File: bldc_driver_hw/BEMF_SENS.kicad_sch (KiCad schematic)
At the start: 4 parts, among them U12 LM397

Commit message: wip
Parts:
- removed R51, R52, R53: R_Small, symbol Device:R_Small
- added C41, C80, C82: 10uF, Capacitor_SMD:C_0805_2012Metric_Pad1.18x1.45mm_HandSolder, symbol Device:C_Small
- added C42, C81, C83: 100nF, Capacitor_SMD:C_0603_1608Metric_Pad1.08x0.95mm_HandSolder, symbol Device:C_Small
- added R78, R79, R80, R81, R82, R83, R84, R85, R86: R_Small, symbol Device:R_Small
- added U13, U14: LM397, Package_TO_SOT_SMD:SOT-23-5, symbol Comparator:LM397
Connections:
- net BEMF_U: now also U12.4
- net BEMF_V: now also U14.4
- net BEMF_W: now also U13.4
- net GND: now also C41.2, C42.2, C80.2, C81.2, C82.2, C83.2, R79.2, R81.2, R85.2, U13.2 (V-), U14.2 (V-)
- net PHASE_U: now also R78.1
- net PHASE_V: now also R84.1
- net PHASE_W: now also R80.1
- net V_BEMF: now also R82.2, R83.2, R86.2, U13.1 (-), U14.1 (-)
- net at U12.3 (+): now also R78.2, R79.1, R82.1
- net +3.3V: now reaches U12.5 (V+)
- net +3.3V: now also C41.1, C42.1, C80.1, C81.1, C82.1, C83.1, U13.5 (V+), U14.5 (V+)
- new net: R80.2, R81.1, R83.1, U13.3 (+)
- new net: R84.2, R85.1, R86.1, U14.3 (+)
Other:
- moved on the sheet: U12

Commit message: schematic finished pcb in progress
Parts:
- removed C81, C83: 100nF, Capacitor_SMD:C_0603_1608Metric_Pad1.08x0.95mm_HandSolder, symbol Device:C_Small
- removed C82: 10uF, Capacitor_SMD:C_0805_2012Metric_Pad1.18x1.45mm_HandSolder, symbol Device:C_Small
- removed R80, R81: R_Small, symbol Device:R_Small
- removed U12, U13, U14: LM397, Package_TO_SOT_SMD:SOT-23-5, symbol Comparator:LM397
- added C78, C79: 27nF, Capacitor_SMD:C_0603_1608Metric, symbol Device:C_Small
- added R100, R98, R99: 10k, Resistor_SMD:R_0603_1608Metric, symbol Device:R_Small
- added R86: 47k, Resistor_SMD:R_0603_1608Metric, symbol Device:R_Small
- added R87: 3k, Resistor_SMD:R_0603_1608Metric, symbol Device:R_Small
- added R89: 100k, Resistor_SMD:R_0603_1608Metric, symbol Device:R
- added R92, R93, R94, R95, R96, R97: R_Small, Resistor_SMD:R_0603_1608Metric, symbol Device:R_Small
- added U13: MCP6569, Package_SO:SOIC-14_3.9x8.7mm_P1.27mm, symbol Comparator:MCP6569
- C80: value 10uF -> 27nF; footprint Capacitor_SMD:C_0805_2012Metric_Pad1.18x1.45mm_HandSolder -> Capacitor_SMD:C_0603_1608Metric; now not fitted
- R82: renamed from R78; value R_Small -> 47k; footprint (none) -> Resistor_SMD:R_0603_1608Metric
- R83: renamed from R79; value R_Small -> 3k; footprint (none) -> Resistor_SMD:R_0603_1608Metric
- R84: value R_Small -> 47k; footprint (none) -> Resistor_SMD:R_0603_1608Metric
- R85: value R_Small -> 3k; footprint (none) -> Resistor_SMD:R_0603_1608Metric
- R88: renamed from R82; value R_Small -> 100k; footprint (none) -> Resistor_SMD:R_0603_1608Metric
- R90: renamed from R83; value R_Small -> 100k; footprint (none) -> Resistor_SMD:R_0603_1608Metric
- R91: renamed from R86; value R_Small -> 100k; footprint (none) -> Resistor_SMD:R_0603_1608Metric
- renumbered C41 to C81, C42 to C82
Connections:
- net +3.3V: now also R100.1, R98.1, R99.1, U13.4 (V+); no longer C80.1
- net BEMF_U: now also R100.2, R96.1, U13.1
- net BEMF_V: now also R95.1, R99.2, U13.8
- net BEMF_W: now also R97.1, R98.2, U13.7
- net GND: now also C78.2, C79.2, R87.2, U13.11 (V-)
- net PHASE_W: now also R86.1
- net V_BEMF: now also U13.2 (-), U13.6 (-), U13.9 (-)
- net at R82.2, R83.1, R88.1: now also C78.1, R93.2
- net at R90.1: now also C80.1, R86.2, R87.1, R94.2
- net at R84.2, R85.1, R91.1: now also C79.1, R92.2
- new net: R92.1, R95.2, U13.10 (+)
- new net: R94.1, R97.2, U13.5 (+)
- new net: R93.1, R96.2, U13.3 (+)
- no-connect marks 0 -> 3
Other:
- moved on the sheet: C81, C82, R90, R91

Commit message: Board finished to review
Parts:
- removed R89: 100k, Resistor_SMD:R_0603_1608Metric, symbol Device:R
- C81: footprint Capacitor_SMD:C_0805_2012Metric_Pad1.18x1.45mm_HandSolder -> Capacitor_SMD:C_0603_1608Metric
- C82: footprint Capacitor_SMD:C_0603_1608Metric_Pad1.08x0.95mm_HandSolder -> Capacitor_SMD:C_0603_1608Metric
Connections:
- net BEMF_V: now also R97.1, R98.2; no longer R95.1, R99.2
- net BEMF_W: now also R95.1, R99.2, U13.14; no longer R97.1, R98.2, U13.7
- net PHASE_V: now also R86.1; no longer R84.1
- net PHASE_W: now also R84.1; no longer R86.1
- net V_BEMF: now also U13.13 (-); no longer U13.6 (-)
- net at R92.1, R95.2: now also U13.12 (+); no longer U13.10 (+)
- net at R94.1, R97.2: now also U13.10 (+); no longer U13.5 (+)
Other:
- moved on the sheet: U13B, U13C, U13D

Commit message: wip
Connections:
- net BEMF_U: now also U13.7; no longer U13.1
- net BEMF_V: now also R95.1, R99.2, U13.14; no longer R97.1, R98.2, U13.8
- net BEMF_W: now also R97.1, R98.2, U13.8; no longer R95.1, R99.2, U13.14
- net PHASE_V: now also R84.1; no longer R86.1
- net PHASE_W: now also R86.1; no longer R84.1
- net V_BEMF: now also U13.6 (-); no longer U13.2 (-)
- net at U13.5 (+): now also R93.1, R96.2
- now unconnected: U13.3 (+)
- no-connect marks 3 -> 0
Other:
- moved on the sheet: U13A, U13B
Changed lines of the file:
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@@
 	)
 	(junction
-		(at 148.59 52.07)
+		(at 182.88 24.13)
 		(diameter 0)
 		(color 0 0 0 0)
 	)
 	(junction
-		(at 182.88 24.13)
+		(at 127 49.53)
 		(diameter 0)
 		(color 0 0 0 0)
@@
 	)
 	(junction
-		(at 127 49.53)
+		(at 109.22 114.3)
 		(diameter 0)
 		(color 0 0 0 0)
 	)
 	(junction
-		(at 109.22 114.3)
+		(at 148.59 52.07)
 		(diameter 0)
 		(color 0 0 0 0)
 	)
-	(no_connect
-		(at 154.94 139.7)
-	)
-	(no_connect
-		(at 139.7 142.24)
-	)
-	(no_connect
-		(at 139.7 137.16)
-	)
 	(wire
 		(pts
@@
 	(wire
 		(pts
-			(xy 114.3 54.61) (xy 133.35 54.61)
-		)
-		(stroke
-			(width 0)
-			(type default)
-		)
-	)
-	(wire
-		(pts
 			(xy 96.52 107.95) (xy 83.82 107.95)
 		)
@@
 	(wire
 		(pts
-			(xy 125.73 49.53) (xy 127 49.53)
-		)
-		(stroke
-			(width 0)
-			(type default)
-		)
-	)
-	(wire
-		(pts
 			(xy 127 106.68) (xy 127 114.3)
 		)
@@
 	(wire
 		(pts
+			(xy 114.3 54.61) (xy 132.08 54.61)
+		)
+		(stroke
+			(width 0)
+			(type default)
+		)
+	)
+	(wire
+		(pts
 			(xy 154.94 109.22) (xy 154.94 116.84)
 		)
@@
 	(wire
 		(pts
-			(xy 97.79 78.74) (xy 97.79 81.28)
+			(xy 127 49.53) (xy 132.08 49.53)
 		)
 		(stroke
@@
 	(wire
 		(pts
-			(xy 162.56 52.07) (xy 156.21 52.07)
+			(xy 97.79 78.74) (xy 97.79 81.28)
 		)
 		(stroke
@@
 	(wire
 		(pts
-			(xy 96.52 107.95) (xy 96.52 110.49)
+			(xy 162.56 52.07) (xy 156.21 52.07)
 		)
 		(stroke
@@
 	(wire
 		(pts
-			(xy 142.24 41.91) (xy 148.59 41.91)
+			(xy 96.52 107.95) (xy 96.52 110.49)
 		)
 		(stroke
@@
 	(wire
 		(pts
-			(xy 127 49.53) (xy 133.35 49.53)
+			(xy 142.24 41.91) (xy 148.59 41.91)
 		)
 		(stroke
@@
 	(wire
 		(pts
+			(xy 125.73 49.53) (xy 127 49.53)
+		)
+		(stroke
+			(width 0)
+			(type default)
+		)
+	)
+	(wire
+		(pts
 			(xy 156.21 52.07) (xy 148.59 52.07)
 		)
@@
 	(wire
 		(pts
+			(xy 147.32 52.07) (xy 148.59 52.07)
+		)
+		(stroke
+			(width 0)
+			(type default)
+		)
+	)
+	(wire
+		(pts
 			(xy 82.55 83.82) (xy 82.55 81.28)
 		)
@@
 			"AAAAAAAJAAAANwADAAgAAAAKAAAA+AACAAwAAAA9AAQABwAAACYAAAAKAAAAPQAEAAcAAAAnAAAA"
 			"CgAAAJQABQAGAAAAKAAAACYAAAAnAAAAuAAFACoAAAArAAAAKAAAACkAAAD3AAMALQAAAAAAAAD6"
-			"AAQAKwAAACwAAAA0AAAA+AACACwAAAA9AAQALg=="
+			"AAQAKwAAACwAAAA0AAAA+AACACwAAAA9AAQALgAAAAAAAAAAAAAAAAAAAAAAAAAAAAAAAAAAAAAA"
+			"AAAAAAAAAAAAAAAAAAAAAAAAAAAAAAAAAAAAAAAAAAAAAAAAAAAAAAAAAAAAAAAAAAAAAAAAAAAA"
+			"AAAAAAAAAAAAAAAAAAAAAAAAAAAAAAAAAAAAAAAAAAAAAAAAAAAAAAAAAAAAAAAAAAAAAAAAAAAA"
+			"AAAAAAAAAAAAAAAAAAAAAAAAAAAAAAAAAAAAAAAAAAAAAAAAAAAAAAAAAAAAAAAAAAAAAAAAAAAA"
+			"AAAAAAAAAAAAAAAAAAAAAAAAAAAAAAAAAAAAAAAAAAAAAAAAAAAAAAAAAAAAAAAAAAAAAAAAAAAA"
+			"AAAAAAAAAAAAAAAAAAAAAAAAAAAAAAAAAAAAAAAAAAAAAAAAAAAAAAAAAAAAAAAAAAAAAAAAAAAA"
+			"AAAAAAAAAAAAAAAAAAAAAAAAAAAAAAAAAAAAAAAAAAAAAAAAAAAAAAAAAAAAAAAAAAAAAAAAAAAA"
+			"AAAAAAAAAAAAAAAAAAAAAAAAAAAAAAAAAAAAAAAAAAAAAAAAAAAAAAAAAAAAAAAAAAAAAAAAAAAA"
+			"AAAAAAAAAAAAAAAAAAAAAAAAAAAAAAAAAAAAAAAAAAAAAAAAAAAAAAAAAAAAAAAAAAAAAAAAAAAA"
+			"AAAAAAAAAAAAAAAAAAAAAAAAAAAAAAAAAAAAAAAAAAAAAAAAAAAAAAAAAAAAAAAAAAAAAAAAAAAA"
+			"AAAAAAAAAAAAAAAAAAAAAAAAAAAAAAAAAAAAAAAAAAAAAAAAAAAAAAAAAAAAAAAAAAAAAAAAAAAA"
+			"AAAAAAAAAAAAAAAAAAAAAAAAAAAAAAAAAAAAAAAAAAAAAAAAAAAAAAAAAAAAAAAAAAAAAAAAAAAA"
+			"AAAAAAAAAAAAAAAAAAAAAAAAAAAAAAAAAAAAAAAAAAAAAAAAAAAAAAAAAAAAAAAAAAAAAAAAAAAA"
+			"AAAAAAAAAAAAAAAAAAAAAAAAAAAAAAAAAAAAAAAAAAAAAAAAAAAAAAAAAAAAAAAAAAAAAAAAAAAA"
+			"AAAAAAAAAAAAAAAAAAAAAAAAAAAAAAAAAAAAAAAAAAAAAAAAAAAAAAAAAAAAAAAAAAAAAAAAAAAA"
+			"AAAAAAAAAAAAAAAAAAAAAAAAAAAAAAAAAAAAAAAAAAAAAAAAAAAAAAAAAAAAAAAAAAAAAAAAAAAA"
+			"AAAAAAAAAAAAAAAAAAAAAAAAAAAAAAAAAAAAAAAAAAAAAAAAAAAAAAAAAAAAAAAAAAAAAAAAAAAA"
+			"AAAAAAAAAAAAAAAAAAAAAAAAAAAAAAAAAAAAAAAAAAAAAAAAAAAAAAAAAAAAAAAAAAAAAAAAAAAA"
+			"AAAAAAAAAAAAAAAAAAAAAAAAAAAAAAAAAAAAACoqACoqKgAqKioAKioqACoqKgCCfoLEgn6C0oN9"
+			"gzgqKioAKioqACoqKgAqKioAKioqACoqKgAqKioAKioqACoqKgAqKioAKioqACoqKgAqKioAKioq"
+			"ACoqKgAqKioAKioqACoqKgBwcQAAAAAAAFAAAAAAAAAAawotzR5cAAAAAAAAXH4AAMC6nQwbXAAA"
+			"AAAAAAAAAAAAAAAAAADwPwAAAAAAAAAAAAAAAAAAAAAQAAAAEAAAACAAAAAAAAAAEQQAAAAAAACg"
+			"p5wMG1wAAEArCA4bXAAAAAAAAAAAAAAAAAAAAAAAAIlTXSAqKioAKioqACoqKgAqKioAKioqACoq"
+			"KgAqKioAKioqAJCQkAGCfoL/gn6C/YJ+gt6Cf4JCKioqAIpRXKeKUVynKioqACoqKgAqKioAKioq"
+			"ACoqKgAqKioAKioqACoqKgCQkJABgn6C/4J+gmuCfoKrgn6C/oJ+gpmJVV+vilJcqioqKgAqKioA"
+			"KioqACoqKgAqKioAKioqACoqKgCDfoKOgn6CqoJ+gv+DfoNmKioqAIJ+glWCfoLqg3t/9odja8Iq"
+			"KioAKioqACoqKgAqKioAKioqACoqKgAqKioAg36CjoJ+gqqCfoL/g36DZioqKgAqKioAhH6EEYN7"
+			"f6aCfoL/gn6CqoR/hBIqKioAKioqACoqKgAqKioAKioqACoqKgCQkJABgn6C/4J+glWCfoKrg36C"
+			"zIN+gsyDfYMhgn6CTIJ+guSCfoLmg36BTyoqKgAqKioAKioqACoqKgAqKioAkJCQAYJ+gv+CfoJV"
+			"gX+BK4J+gjOCfoIzg4ODCCoqKgCDfIMQgn6CmYJ+gv+CfoKqhYCAEyoqKgAqKioAKioqAJCQkAGC"
+			"foL/gn6CVSoqKgAqKioAKioqACoqKgAqKioAKioqACoqKgCCf4JOgn6C5oJ+gvKCfoK5g36Cjioq"
+			"KgCQkJABgn6C/4J+glUqKioAgn6C14N+gykqKioAKioqACoqKgAqKioAgn+CToJ+guaCfoLygn6C"
+			"uYN+go4qKioAkJCQAYJ+gv+CfoJWgn6C3YJ+gvqCfoLign6CRSoqKgCDfIMQgn6CmYJ+gv+CfoKq"
+			"hYCAEyoqKgAqKioAKioqAJCQkAGCfoL/gn6CVYR+gSKDfoLcgn2BRoGBgQ6CfoJMgn6C5YJ+guaD"
+			"foFPKioqACoqKgAqKioAKioqAIN+go6CfoKqgn6C/4J+gmQqKioAg36DR4F+gSKDe3+ugn6C/4J+"
+			"gqqEf4QSKioqACoqKgAqKioAKioqACoqKgCDfoKOgn6CqoJ+gv+CfoJkKioqAIJ+glWCfoLqg3t/"
+			"9odja8IqKioAKioqACoqKgAqKioAKioqACoqKg=="
 		)
 	)
@@
 	(hierarchical_label "BEMF_V"
 		(shape output)
-		(at 162.56 83.82 0)
+		(at 161.29 116.84 0)
 		(effects
 			(font
@@
 		)
 	)
-	(hierarchical_label "PHASE_V"
-		(shape input)
-		(at 85.09 71.12 180)
+	(hierarchical_label "BEMF_W"
+		(shape output)
+		(at 162.56 83.82 0)
 		(effects
 			(font
 				(size 1.27 1.27)
 			)
-			(justify right)
+			(justify left)
 		)
 	)
-	(hierarchical_label "PHASE_W"
-		(shape input)
-		(at 83.82 107.95 180)
+	(hierarchical_label "BEMF_U"
+		(shape output)
+		(at 162.56 52.07 0)
 		(effects
 			(font
 				(size 1.27 1.27)
 			)
-			(justify right)
+			(justify left)
 		)
 	)
-	(hierarchical_label "BEMF_U"
-		(shape output)
-		(at 162.56 52.07 0)
+	(hierarchical_label "PHASE_V"
+		(shape input)
+		(at 83.82 107.95 180)
 		(effects
 			(font
 				(size 1.27 1.27)
 			)
-			(justify left)
+			(justify right)
 		)
 	)
@@
 		)
 	)
-	(hierarchical_label "BEMF_W"
-		(shape output)
-		(at 161.29 116.84 0)
+	(hierarchical_label "PHASE_W"
+		(shape input)
+		(at 85.09 71.12 180)
 		(effects
 			(font
 				(size 1.27 1.27)
 			)
-			(justify left)
+			(justify right)
 		)
 	)
@@
 	(symbol
 		(lib_id "Comparator:MCP6569")
-		(at 147.32 139.7 0)
+		(at 139.7 52.07 0)
 		(unit 2)
 		(exclude_from_sim no)
@@
 		(dnp no)
 		(property "Reference" "U13"
-			(at 149.098 144.78 0)
+			(at 141.478 57.15 0)
 			(effects
 				(font
@@
 		)
 		(property "Value" "MCP6569"
-			(at 149.098 147.32 0)
+			(at 141.478 59.69 0)
 			(effects
 				(font
@@
 		)
 		(property "Footprint" "Package_SO:SOIC-14_3.9x8.7mm_P1.27mm"
-			(at 146.05 137.16 0)
+			(at 138.43 49.53 0)
 			(effects
 				(font
@@
 		)
 		(property "Datasheet" "http://ww1.microchip.com/downloads/en/DeviceDoc/MCP6566-6R-6U-7-9-1.8V-Low-Power-Open-Drain-Output-Comparator-DS20002143G.pdf"
-			(at 148.59 134.62 0)
+			(at 140.97 46.99 0)
 			(effects
 				(font
@@
 		)
 		(property "Description" "Quad 1.8V Low-Power Open-Drain Output Comparator, SOIC-14/TSSOP-14"
-			(at 147.32 139.7 0)
+			(at 139.7 52.07 0)
 			(effects
 				(font
@@
 		)
 		(property "Description_1" ""
-			(at 147.32 139.7 0)
+			(at 139.7 52.07 0)
 			(effects
 				(font
@@
 		)
 		(property "Height" ""
-			(at 147.32 139.7 0)
+			(at 139.7 52.07 0)
 			(effects
 				(font
@@
 		)
 		(property "Manufacturer_Name" ""
-			(at 147.32 139.7 0)
+			(at 139.7 52.07 0)
 			(effects
 				(font
@@
 		)
 		(property "Manufacturer_Part_Number" ""
-			(at 147.32 139.7 0)
+			(at 139.7 52.07 0)
 			(effects
 				(font
@@
 		)
 		(property "Mouser Part Number" ""
-			(at 147.32 139.7 0)
+			(at 139.7 52.07 0)
 			(effects
 				(font
@@
 		)
 		(property "Mouser Price/Stock" ""
-			(at 147.32 139.7 0)
+			(at 139.7 52.07 0)
 			(effects
 				(font
@@
 	(symbol
 		(lib_id "Comparator:MCP6569")
-		(at 140.97 52.07 0)
+		(at 236.22 77.47 0)
 		(unit 1)
 		(exclude_from_sim no)
@@
 		(dnp no)
 		(property "Reference" "U13"
-			(at 123.952 35.56 0)
+			(at 219.202 60.96 0)
 			(effects
 				(font
@@
 		)
 		(property "Value" "MCP6569"
-			(at 123.952 38.1 0)
+			(at 219.202 63.5 0)
 			(effects
 				(font
@@
 		)
 		(property "Footprint" "Package_SO:SOIC-14_3.9x8.7mm_P1.27mm"
-			(at 139.7 49.53 0)
+			(at 234.95 74.93 0)
 			(effects
 				(font
@@
 		)
 		(property "Datasheet" "http://ww1.microchip.com/downloads/en/DeviceDoc/MCP6566-6R-6U-7-9-1.8V-Low-Power-Open-Drain-Output-Comparator-DS20002143G.pdf"
-			(at 142.24 46.99 0)
+			(at 237.49 72.39 0)
 			(effects
 				(font
@@
 		)
 		(property "Description" "Quad 1.8V Low-Power Open-Drain Output Comparator, SOIC-14/TSSOP-14"
-			(at 140.97 52.07 0)
+			(at 236.22 77.47 0)
 			(effects
 				(font
@@
 		)
 		(property "Description_1" ""
-			(at 140.97 52.07 0)
+			(at 236.22 77.47 0)
 			(effects
 				(font
@@
 		)
 		(property "Height" ""
-			(at 140.97 52.07 0)
+			(at 236.22 77.47 0)
 			(effects
 				(font
@@
 		)
 		(property "Manufacturer_Name" ""
-			(at 140.97 52.07 0)
+			(at 236.22 77.47 0)
 			(effects
 				(font
@@
 		)
 		(property "Manufacturer_Part_Number" ""
-			(at 140.97 52.07 0)
+			(at 236.22 77.47 0)
 			(effects
 				(font
@@
 		)
 		(property "Mouser Part Number" ""
-			(at 140.97 52.07 0)
+			(at 236.22 77.47 0)
 			(effects
 				(font
@@
 		)
 		(property "Mouser Price/Stock" ""
-			(at 140.97 52.07 0)
+			(at 236.22 77.47 0)
 			(effects
 				(font

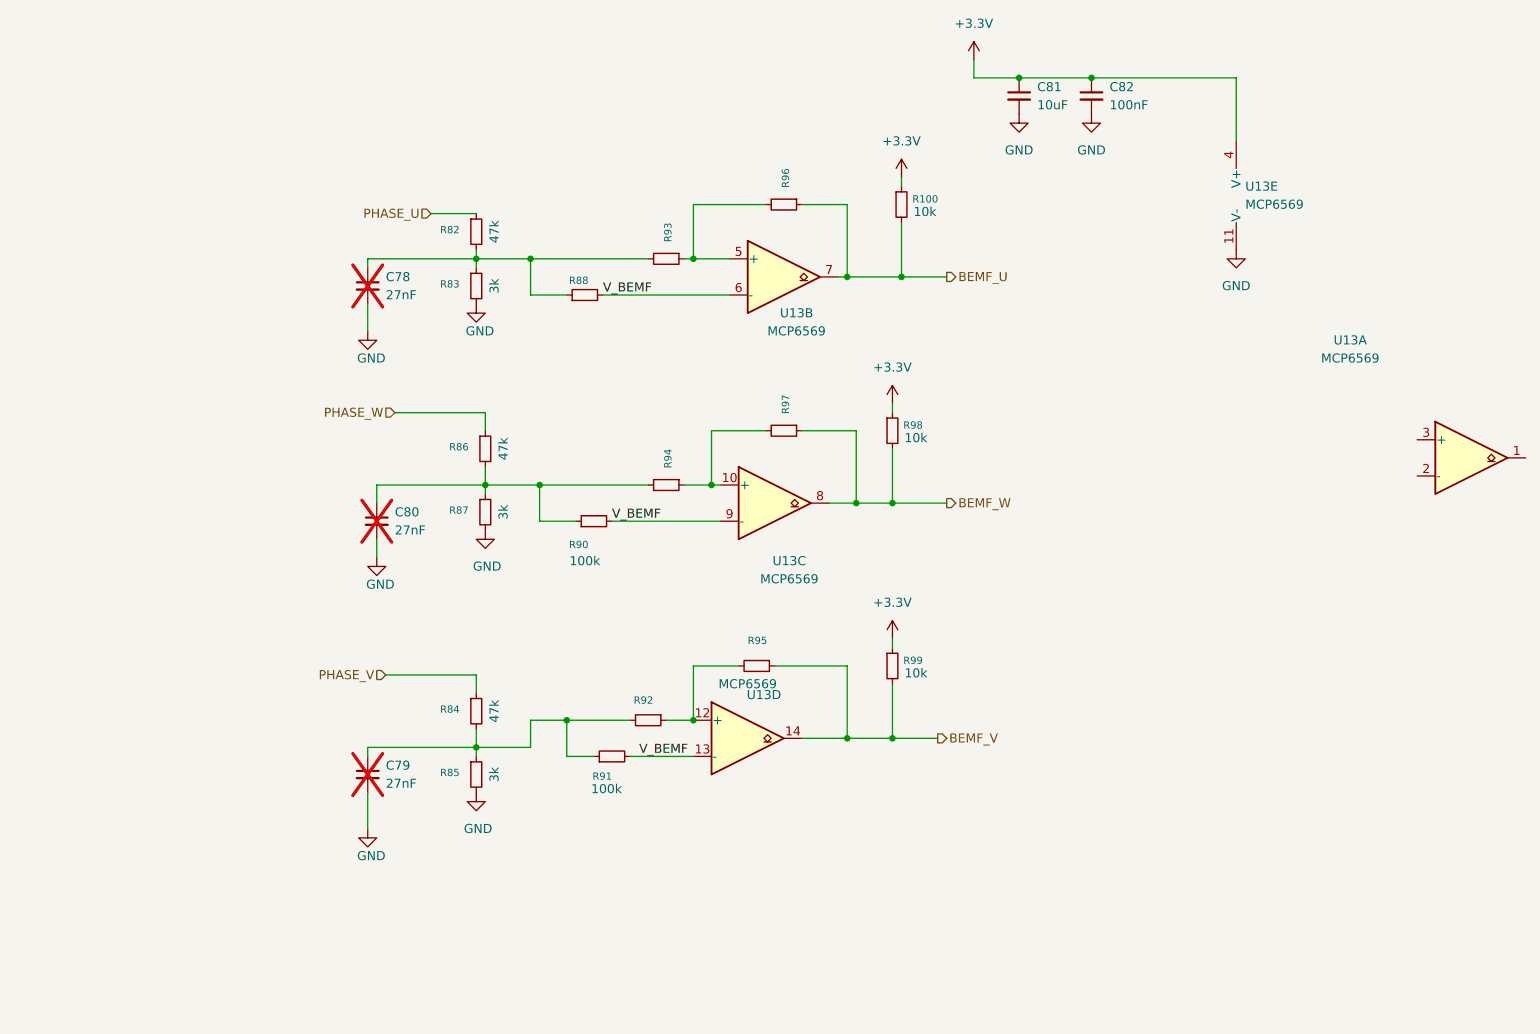
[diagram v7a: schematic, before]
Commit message: added lcsc codes
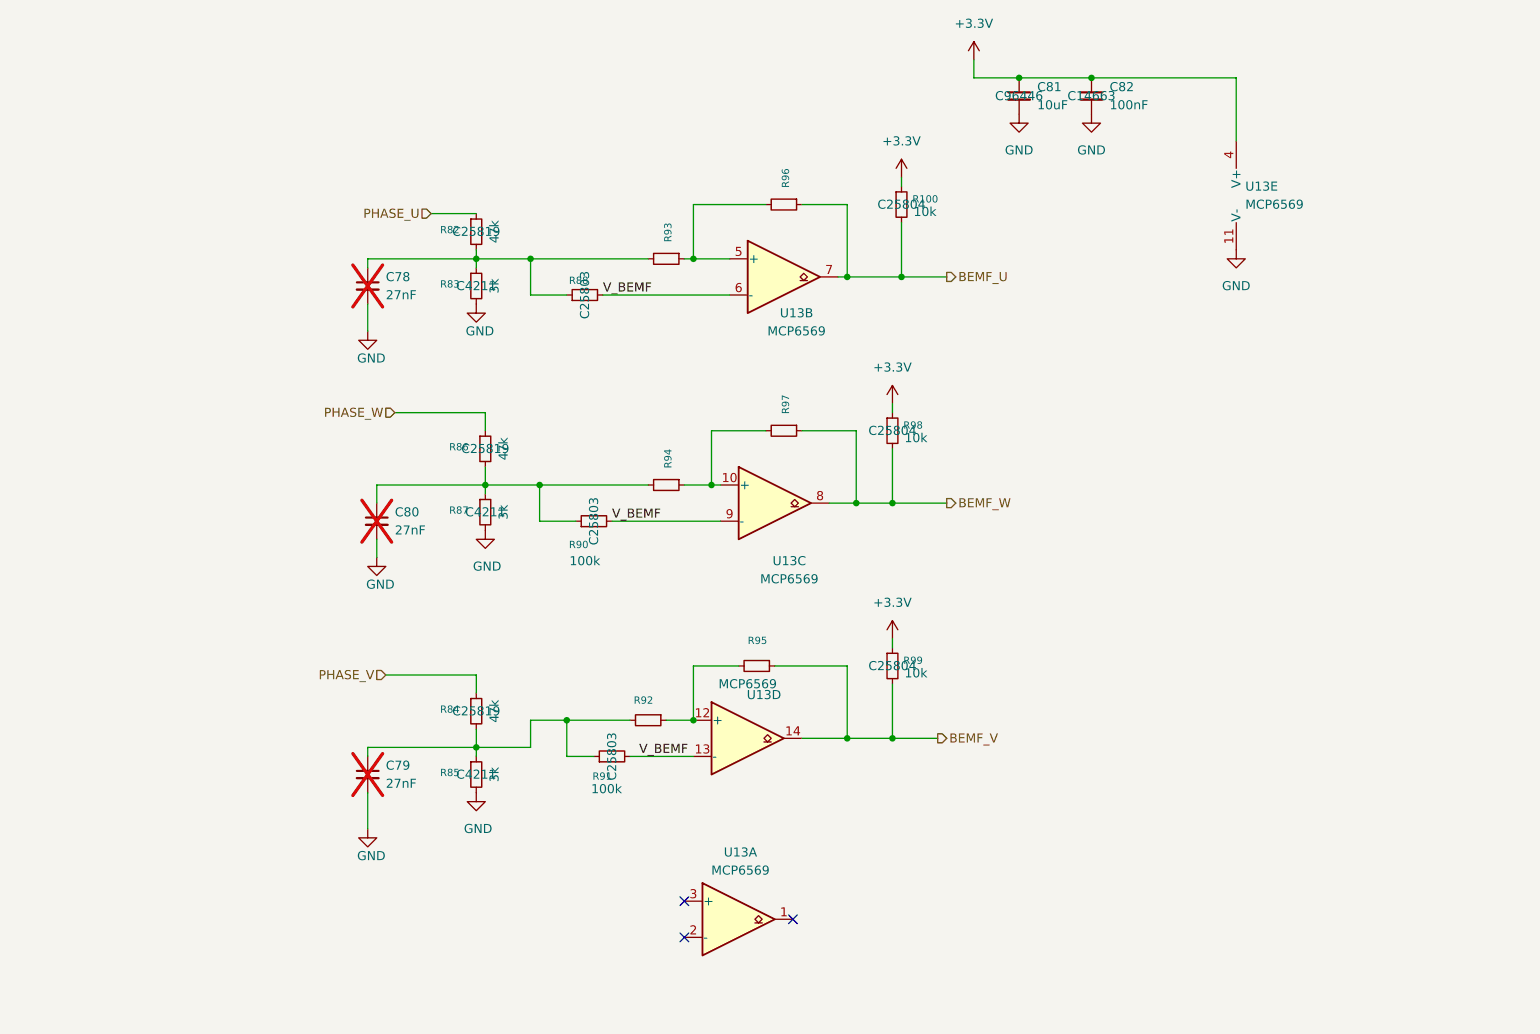
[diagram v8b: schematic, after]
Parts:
- C81: LCSC (none) -> C96446
- C82: LCSC (none) -> C14663
- R100, R98, R99: LCSC (none) -> C25804
- R82, R84, R86: LCSC (none) -> C25819
- R83, R85, R87: LCSC (none) -> C4211
- R88, R90, R91: LCSC (none) -> C25803
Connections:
- no-connect marks 0 -> 3
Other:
- moved on the sheet: U13A
